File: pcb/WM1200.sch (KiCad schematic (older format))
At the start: 0 parts

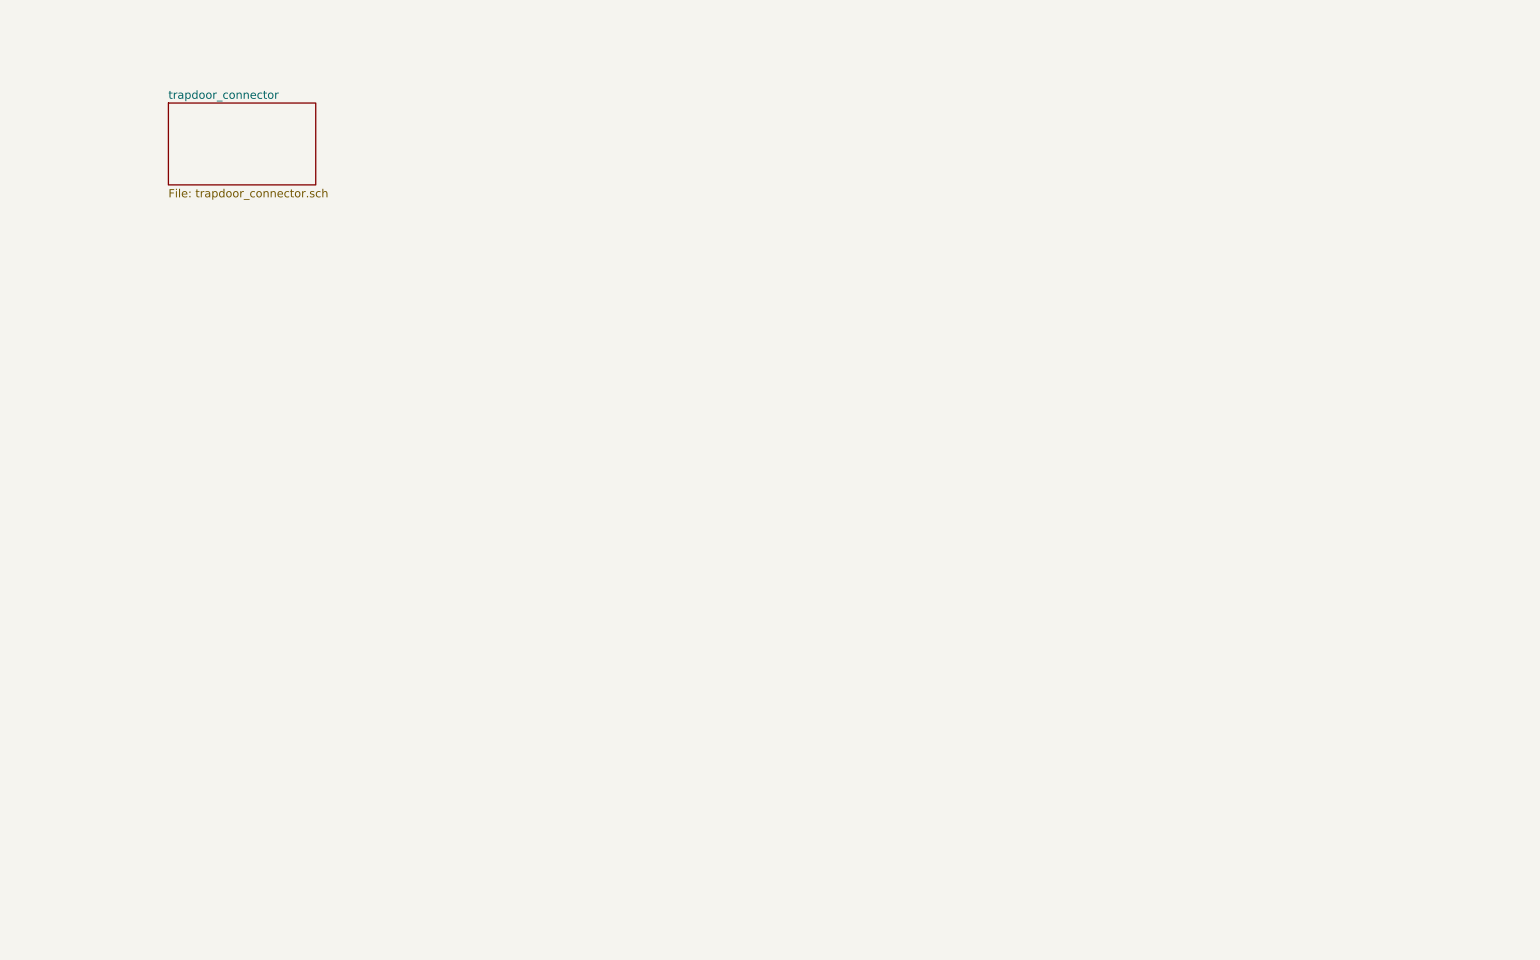
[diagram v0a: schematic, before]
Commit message: hierarchy updated
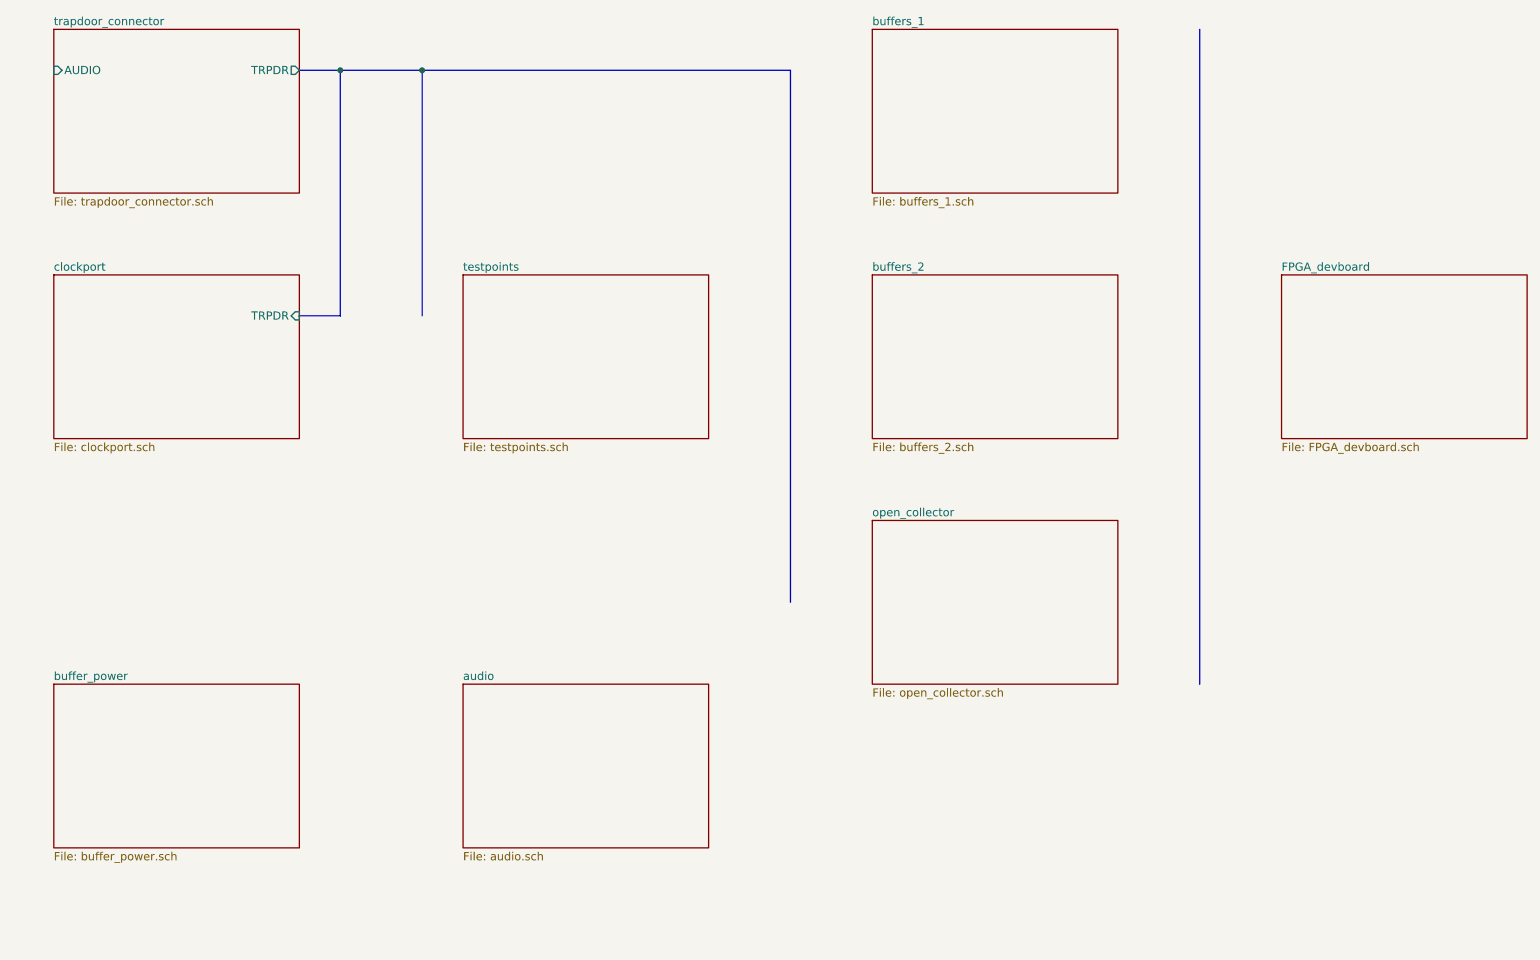
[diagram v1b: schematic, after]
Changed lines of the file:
@@
 $Descr A4 11693 8268
 encoding utf-8
-Sheet 1 2
+Sheet 1 10
 Title "WishMaster 1200"
 Date ""
@@
 $EndDescr
 $Sheet
-S 1700 1450 900  500
+S 1000 1000 1500 1000
 U 5E6286C8
 F0 "trapdoor_connector" 50
 F1 "trapdoor_connector.sch" 50
+F2 "TRPDR" O R 2500 1250 50
+F3 "AUDIO" I L 1000 1250 50
+$EndSheet
+$Sheet
+S 1000 2500 1500 1000
+U 5E55E8C3
+F0 "clockport" 50
+F1 "clockport.sch" 50
+F2 "TRPDR" I R 2500 2750 50
+$EndSheet
+Wire Bus Line
+	2500 1250 2750 1250
+$Sheet
+S 3500 2500 1500 1000
+U 5E5B86AA
+F0 "testpoints" 50
+F1 "testpoints.sch" 50
+$EndSheet
+$Sheet
+S 6000 1000 1500 1000
+U 5E5B89F7
+F0 "buffers_1" 50
+F1 "buffers_1.sch" 50
+$EndSheet
+$Sheet
+S 6000 2500 1500 1000
+U 5E5B8B5B
+F0 "buffers_2" 50
+F1 "buffers_2.sch" 50
+$EndSheet
+Wire Bus Line
+	2750 1250 2750 2750
+Wire Bus Line
+	2750 2750 2500 2750
+Connection ~ 2750 1250
+Wire Bus Line
+	2750 1250 3250 1250
+$Sheet
+S 6000 4000 1500 1000
+U 5E5B9D2E
+F0 "open_collector" 50
+F1 "open_collector.sch" 50
+$EndSheet
+$Sheet
+S 8500 2500 1500 1000
+U 5E5BA060
+F0 "FPGA_devboard" 50
+F1 "FPGA_devboard.sch" 50
+$EndSheet
+Wire Bus Line
+	3250 2750 3250 1250
+Connection ~ 3250 1250
+Wire Bus Line
+	5500 1250 5500 4500
+Wire Bus Line
+	3250 1250 5500 1250
+Wire Bus Line
+	8000 1000 8000 5000
+$Sheet
+S 1000 5000 1500 1000
+U 5E5BBEAC
+F0 "buffer_power" 50
+F1 "buffer_power.sch" 50
+$EndSheet
+$Sheet
+S 3500 5000 1500 1000
+U 5E5BC361
+F0 "audio" 50
+F1 "audio.sch" 50
 $EndSheet
 $EndSCHEMATC

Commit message: some work on sheets
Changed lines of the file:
@@
 $EndDescr
 $Sheet
-S 1000 1000 1500 1000
+S 1000 1000 1500 500
 U 5E6286C8
 F0 "trapdoor_connector" 50
 F1 "trapdoor_connector.sch" 50
-F2 "TRPDR" O R 2500 1250 50
+F2 "TRPDR" O R 2500 1150 50
 F3 "AUDIO" I L 1000 1250 50
+F4 "POWER_GND" O R 2500 1350 50
 $EndSheet
 $Sheet
-S 1000 2500 1500 1000
+S 3500 1500 1500 500
 U 5E55E8C3
 F0 "clockport" 50
 F1 "clockport.sch" 50
-F2 "TRPDR" I R 2500 2750 50
+F2 "TRPDR" I L 3500 1750 50
 $EndSheet
 Wire Bus Line
-	2500 1250 2750 1250
+	2500 1150 3000 1150
 $Sheet
-S 3500 2500 1500 1000
+S 3500 2500 1500 500
 U 5E5B86AA
 F0 "testpoints" 50
 F1 "testpoints.sch" 50
 $EndSheet
+Wire Bus Line
+	3000 1150 3000 1750
+Wire Bus Line
+	3000 1750 3500 1750
+Connection ~ 3000 1150
 $Sheet
-S 6000 1000 1500 1000
-U 5E5B89F7
-F0 "buffers_1" 50
-F1 "buffers_1.sch" 50
-$EndSheet
-$Sheet
-S 6000 2500 1500 1000
-U 5E5B8B5B
-F0 "buffers_2" 50
-F1 "buffers_2.sch" 50
-$EndSheet
-Wire Bus Line
-	2750 1250 2750 2750
-Wire Bus Line
-	2750 2750 2500 2750
-Connection ~ 2750 1250
-Wire Bus Line
-	2750 1250 3250 1250
-$Sheet
-S 6000 4000 1500 1000
+S 6000 4500 1500 500
 U 5E5B9D2E
 F0 "open_collector" 50
@@
 $EndSheet
 Wire Bus Line
-	3250 2750 3250 1250
-Connection ~ 3250 1250
+	5500 1150 5500 1650
 Wire Bus Line
-	5500 1250 5500 4500
-Wire Bus Line
-	3250 1250 5500 1250
-Wire Bus Line
-	8000 1000 8000 5000
+	8000 1000 8000 1750
 $Sheet
-S 1000 5000 1500 1000
-U 5E5BBEAC
-F0 "buffer_power" 50
-F1 "buffer_power.sch" 50
-$EndSheet
-$Sheet
-S 3500 5000 1500 1000
+S 3000 6000 1500 500
 U 5E5BC361
 F0 "audio" 50
 F1 "audio.sch" 50
+F2 "AUDIO" O L 3000 6250 50
+F3 "FGPA" I R 4500 6250 50
 $EndSheet
+$Sheet
+S 6000 1500 1450 500
+U 5E5B89F7
+F0 "buffers_data" 50
+F1 "buffers_data.sch" 50
+F2 "FPGA" B R 7450 1750 50
+F3 "TRPDR" B L 6000 1650 50
+F4 "POWER_GND" I L 6000 1850 50
+$EndSheet
+$Sheet
+S 6000 2500 1500 500
+U 5E78104B
+F0 "buffers_addr" 50
+F1 "buffers_addr.sch" 50
+F2 "FPGA" B R 7500 2750 50
+F3 "TRPDR" B L 6000 2650 50
+F4 "POWER_GND" I L 6000 2850 50
+$EndSheet
+$Sheet
+S 6000 3500 1500 500
+U 5E78B6EB
+F0 "buffers_system_zorroii" 50
+F1 "buffers_system_zorroii.sch" 50
+F2 "FPGA" B R 7500 3750 50
+F3 "TRPDR" B L 6000 3650 50
+F4 "POWER_GND" I L 6000 3850 50
+$EndSheet
+Wire Bus Line
+	1000 1250 750  1250
+Wire Bus Line
+	750  1250 750  6250
+Wire Bus Line
+	750  6250 3000 6250
+Wire Bus Line
+	3000 1150 5500 1150
+Connection ~ 3000 1750
+Wire Bus Line
+	3000 1750 3000 3250
+Wire Bus Line
+	5750 1350 5750 1850
+Wire Bus Line
+	2500 1350 3200 1350
+Wire Bus Line
+	5500 1650 6000 1650
+Connection ~ 5500 1650
+Wire Bus Line
+	5500 1650 5500 2650
+Wire Bus Line
+	6000 1850 5750 1850
+Connection ~ 5750 1850
+Wire Bus Line
+	5750 1850 5750 2850
+Wire Bus Line
+	6000 2650 5500 2650
+Connection ~ 5500 2650
+Wire Bus Line
+	6000 2850 5750 2850
+Connection ~ 5750 2850
+Wire Bus Line
+	5750 2850 5750 3850
+Wire Bus Line
+	6000 3650 5500 3650
+Wire Bus Line
+	5500 2650 5500 3650
+Connection ~ 5500 3650
+Wire Bus Line
+	5500 3650 5500 4500
+Wire Bus Line
+	6000 3850 5750 3850
+Connection ~ 5750 3850
+Wire Bus Line
+	5750 3850 5750 5000
+Wire Bus Line
+	3200 1350 3200 3500
+Connection ~ 3200 1350
+Wire Bus Line
+	3200 1350 5750 1350
+Wire Bus Line
+	7450 1750 8000 1750
+Connection ~ 8000 1750
+Wire Bus Line
+	7500 2750 8000 2750
+Wire Bus Line
+	8000 1750 8000 2750
+Connection ~ 8000 2750
+Wire Bus Line
+	8000 2750 8000 3750
+Wire Bus Line
+	7500 3750 8000 3750
+Connection ~ 8000 3750
+Wire Bus Line
+	4500 6250 8000 6250
+Wire Bus Line
+	8000 3750 8000 6250
 $EndSCHEMATC
